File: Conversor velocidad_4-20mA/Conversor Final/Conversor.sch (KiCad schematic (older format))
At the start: 32 parts, among them J1 Bornera Señal de Entrada, J2 Bornera continua > 15V, J3 Salida 4-20mA, Q1 BC848, Q2 PN2222A, U1 L7815, U2 4040, U3 4070, U4 TL082, U5 TL082

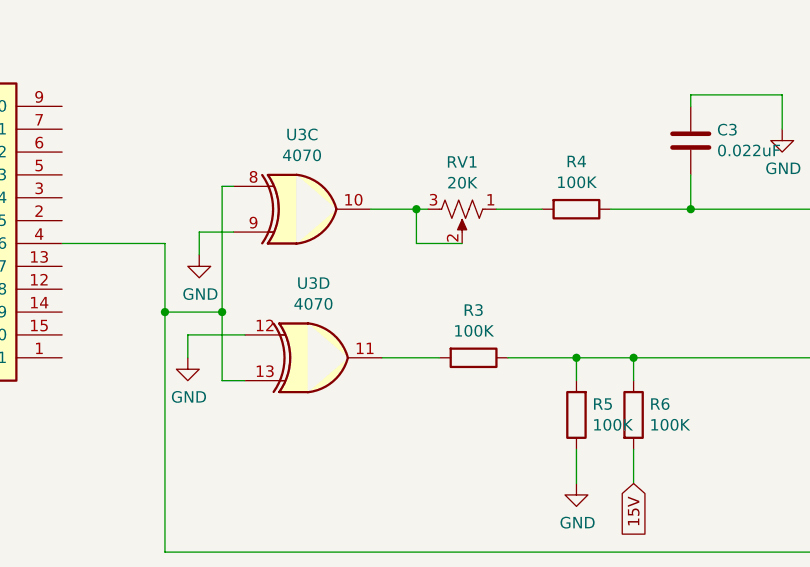
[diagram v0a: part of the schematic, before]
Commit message: Arreglo esquemático
Agrego el puente que hay entre los pines 10 y 11 del 4070
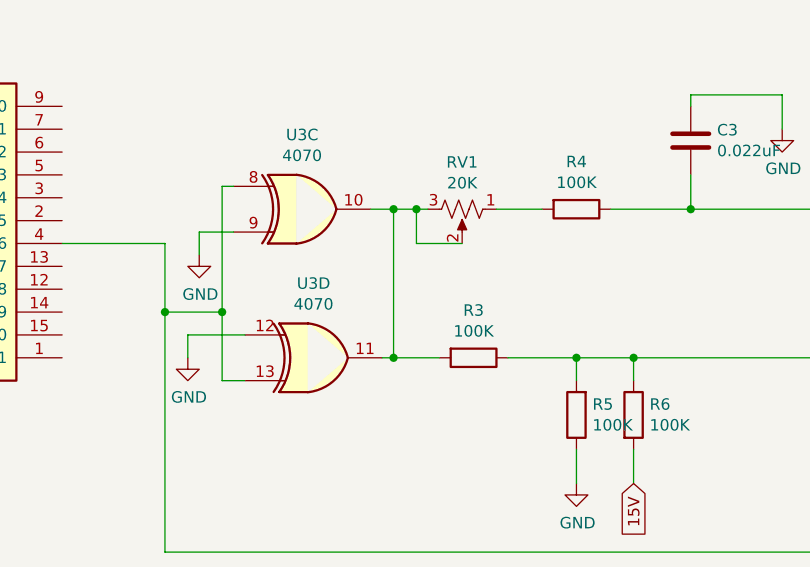
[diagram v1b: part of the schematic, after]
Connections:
- net at RV1.2, RV1.3, U3.10: now also R3.2, U3.11
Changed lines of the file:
@@
 $EndComp
 Wire Wire Line
-	5250 3350 5450 3350
-Wire Wire Line
-	5300 4000 5550 4000
+	5250 3350 5350 3350
+Wire Wire Line
+	5300 4000 5350 4000
 Wire Wire Line
 	4600 3250 4600 3800
@@
 Wire Wire Line
 	2050 6100 2200 6100
+Wire Wire Line
+	5350 3350 5350 4000
+Connection ~ 5350 3350
+Wire Wire Line
+	5350 3350 5450 3350
+Connection ~ 5350 4000
+Wire Wire Line
+	5350 4000 5550 4000
 $EndSCHEMATC
